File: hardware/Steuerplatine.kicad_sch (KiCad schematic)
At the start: 9 parts, among them J1 Conn_01x02_Pin, J2 Conn_01x02_Pin, J3 Conn_01x06_Pin

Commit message: done routing
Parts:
- removed J3: Conn_01x06_Pin, Connector_Phoenix_MC:PhoenixContact_MC_1,5_6-G-3.5_1x06_P3.50mm_Horizontal, symbol Connector:Conn_01x06_Pin
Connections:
- net L: now also J1.2 (Pin_2); no longer J1.1 (Pin_1)
- net N: now also J1.1 (Pin_1); no longer J1.2 (Pin_2)
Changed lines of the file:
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@@
 		)
 	)
-	(label "GND"
-		(at 254 124.46 180)
+	(label "+5V"
+		(at 245.11 21.59 0)
 		(fields_autoplaced yes)
 		(effects
@@
 				(size 1.27 1.27)
 			)
-			(justify right bottom)
-		)
-	)
-	(label "+5V"
-		(at 245.11 21.59 0)
+			(justify left bottom)
+		)
+	)
+	(label "L"
+		(at 245.11 29.21 0)
 		(fields_autoplaced yes)
 		(effects
@@
 	)
 	(label "+5V"
-		(at 254 127 180)
+		(at 41.91 21.59 0)
 		(fields_autoplaced yes)
 		(effects
@@
 				(size 1.27 1.27)
 			)
-			(justify right bottom)
-		)
-	)
-	(label "L"
-		(at 245.11 29.21 0)
-		(fields_autoplaced yes)
-		(effects
-			(font
-				(size 1.27 1.27)
-			)
-			(justify left bottom)
-		)
-	)
-	(label "+5V"
-		(at 41.91 21.59 0)
-		(fields_autoplaced yes)
-		(effects
-			(font
-				(size 1.27 1.27)
-			)
 			(justify left bottom)
 		)
@@
 	)
 	(symbol
-		(lib_id "Connector:Conn_01x06_Pin")
-		(at 259.08 121.92 180)
-		(unit 1)
-		(exclude_from_sim no)
-		(in_bom yes)
-		(on_board yes)
-		(dnp no)
-		(fields_autoplaced yes)
-		(property "Reference" "J3"
-			(at 260.35 119.3799 0)
-			(effects
-				(font
-					(size 1.27 1.27)
-				)
-				(justify right)
-			)
-		)
-		(property "Value" "Conn_01x06_Pin"
-			(at 260.35 121.9199 0)
-			(effects
-				(font
-					(size 1.27 1.27)
-				)
-				(justify right)
-			)
-		)
-		(property "Footprint" "Connector_Phoenix_MC:PhoenixContact_MC_1,5_6-G-3.5_1x06_P3.50mm_Horizontal"
-			(at 259.08 121.92 0)
-			(effects
-				(font
-					(size 1.27 1.27)
-				)
-				(hide yes)
-			)
-		)
-		(property "Datasheet" "~"
-			(at 259.08 121.92 0)
-			(effects
-				(font
-					(size 1.27 1.27)
-				)
-				(hide yes)
-			)
-		)
-		(property "Description" "Generic connector, single row, 01x06, script generated"
-			(at 259.08 121.92 0)
-			(effects
-				(font
-					(size 1.27 1.27)
-				)
-				(hide yes)
-			)
-		)
-		(pin "4"
-		)
-		(pin "3"
-		)
-		(pin "2"
-		)
-		(pin "1"
-		)
-		(pin "5"
-		)
-		(pin "6"
-		)
-		(instances
-			(project "Steuerplatine"
-				(path "/ae153005-c1c4-4678-92de-98a47cf88e8d"
-					(reference "J3")
-					(unit 1)
-				)
-			)
-		)
-	)
-	(symbol
 		(lib_id "Mechanical:MountingHole")
 		(at 16.51 193.04 0)
@@
 	(symbol
 		(lib_id "Connector:Conn_01x02_Pin")
-		(at 35.56 29.21 0)
+		(at 35.56 31.75 0)
+		(mirror x)
 		(unit 1)
 		(exclude_from_sim no)
@@
 		(dnp no)
 		(property "Reference" "J1"
-			(at 32.512 31.242 0)
+			(at 32.512 29.718 0)
 			(effects
 				(font
@@
 		)
 		(property "Value" "Conn_01x02_Pin"
-			(at 22.606 31.242 0)
+			(at 22.606 29.718 0)
 			(effects
 				(font
@@
 		)
 		(property "Footprint" "Connector_Phoenix_GMSTB:PhoenixContact_GMSTBA_2,5_2-G-7,62_1x02_P7.62mm_Horizontal"
-			(at 35.56 29.21 0)
-			(effects
-				(font
-					(size 1.27 1.27)
-				)
-				(hide yes)
-			)
-		)
-		(property "Datasheet" "~"
-			(at 35.56 29.21 0)
+			(at 35.56 31.75 0)
+			(effects
+				(font
+					(size 1.27 1.27)
+				)
+				(hide yes)
+			)
+		)
+		(property "Datasheet" "~"
+			(at 35.56 31.75 0)
 			(effects
 				(font
@@
 		)
 		(property "Description" "Generic connector, single row, 01x02, script generated"
-			(at 35.56 29.21 0)
-			(effects
-				(font
+			(at 35.56 31.75 0)
+			(effects
+				(font

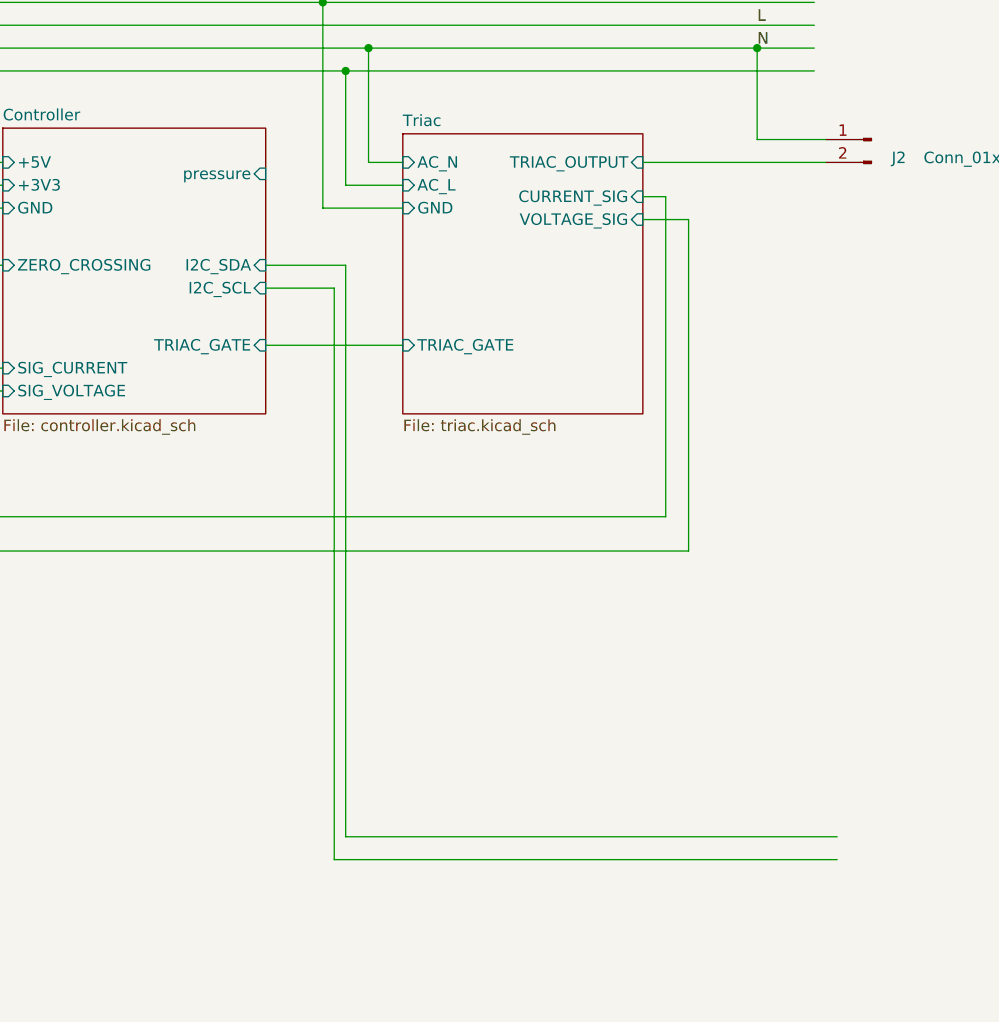
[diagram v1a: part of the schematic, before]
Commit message: added pressure sensor
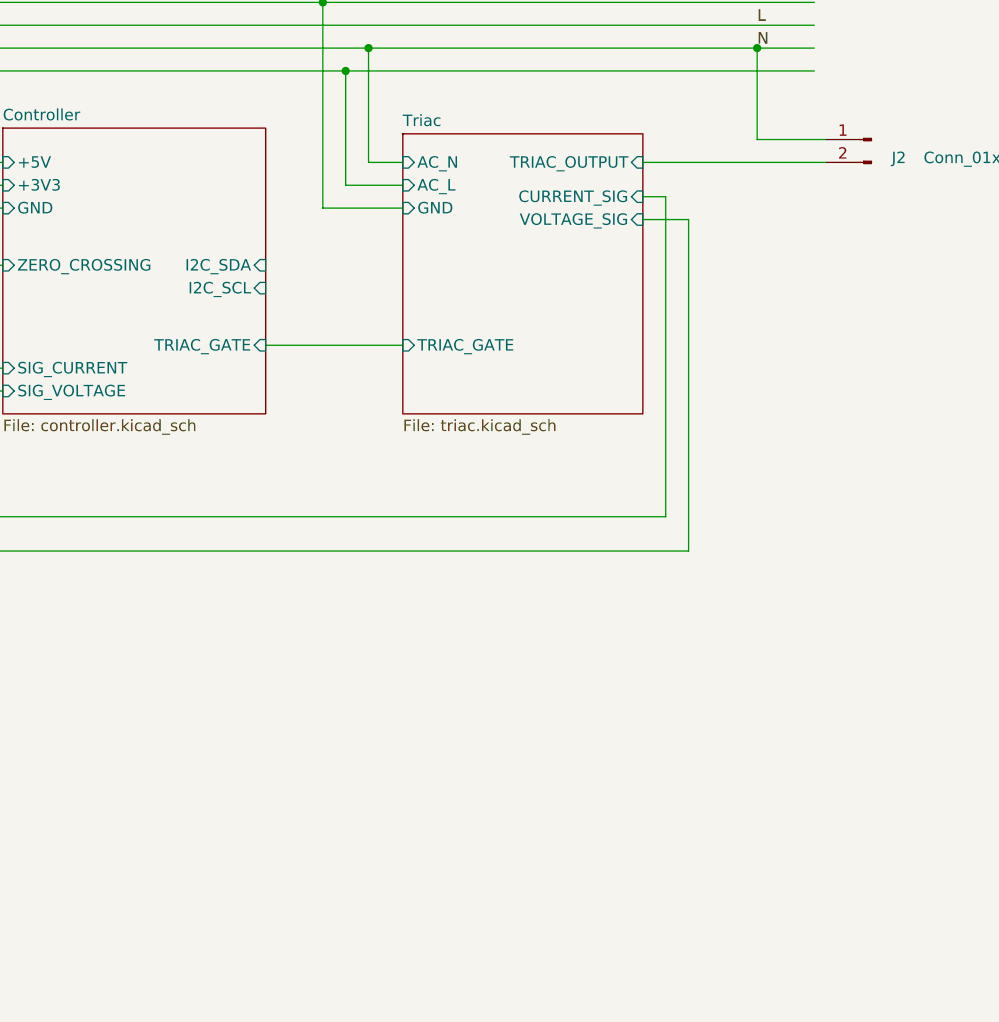
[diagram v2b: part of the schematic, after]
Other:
- sheet Controller ports: added none; removed pressure
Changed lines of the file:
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@@
-	(wire
-		(pts
-			(xy 190.5 58.42) (xy 198.12 58.42)
-		)
-		(stroke
-			(width 0)
-			(type default)
-		)
-	)
 	(wire
 		(pts
@@
 	(wire
 		(pts
-			(xy 190.5 55.88) (xy 199.39 55.88)
-		)
-		(stroke
-			(width 0)
-			(type default)
-		)
-	)
-	(wire
-		(pts
 			(xy 104.14 34.29) (xy 104.14 55.88)
 		)
@@
 	(wire
 		(pts
-			(xy 199.39 55.88) (xy 199.39 119.38)
-		)
-		(stroke
-			(width 0)
-			(type default)
-		)
-	)
-	(wire
-		(pts
-			(xy 198.12 121.92) (xy 254 121.92)
-		)
-		(stroke
-			(width 0)
-			(type default)
-		)
-	)
-	(wire
-		(pts
 			(xy 152.4 26.67) (xy 152.4 49.53)
 		)
@@
 	(wire
 		(pts
-			(xy 199.39 119.38) (xy 254 119.38)
-		)
-		(stroke
-			(width 0)
-			(type default)
-		)
-	)
-	(wire
-		(pts
 			(xy 40.64 34.29) (xy 76.2 34.29)
 		)
@@
 		(pts
 			(xy 237.49 87.63) (xy 158.75 87.63)
-		)
-		(stroke
-			(width 0)
-			(type default)
-		)
-	)
-	(wire
-		(pts
-			(xy 198.12 58.42) (xy 198.12 121.92)
 		)
 		(stroke
@@
 			)
 		)
-		(pin "pressure" input
-			(at 190.5 45.72 0)
-			(effects
-				(font
-					(size 1.27 1.27)
-				)
-				(justify right)
-			)
-		)

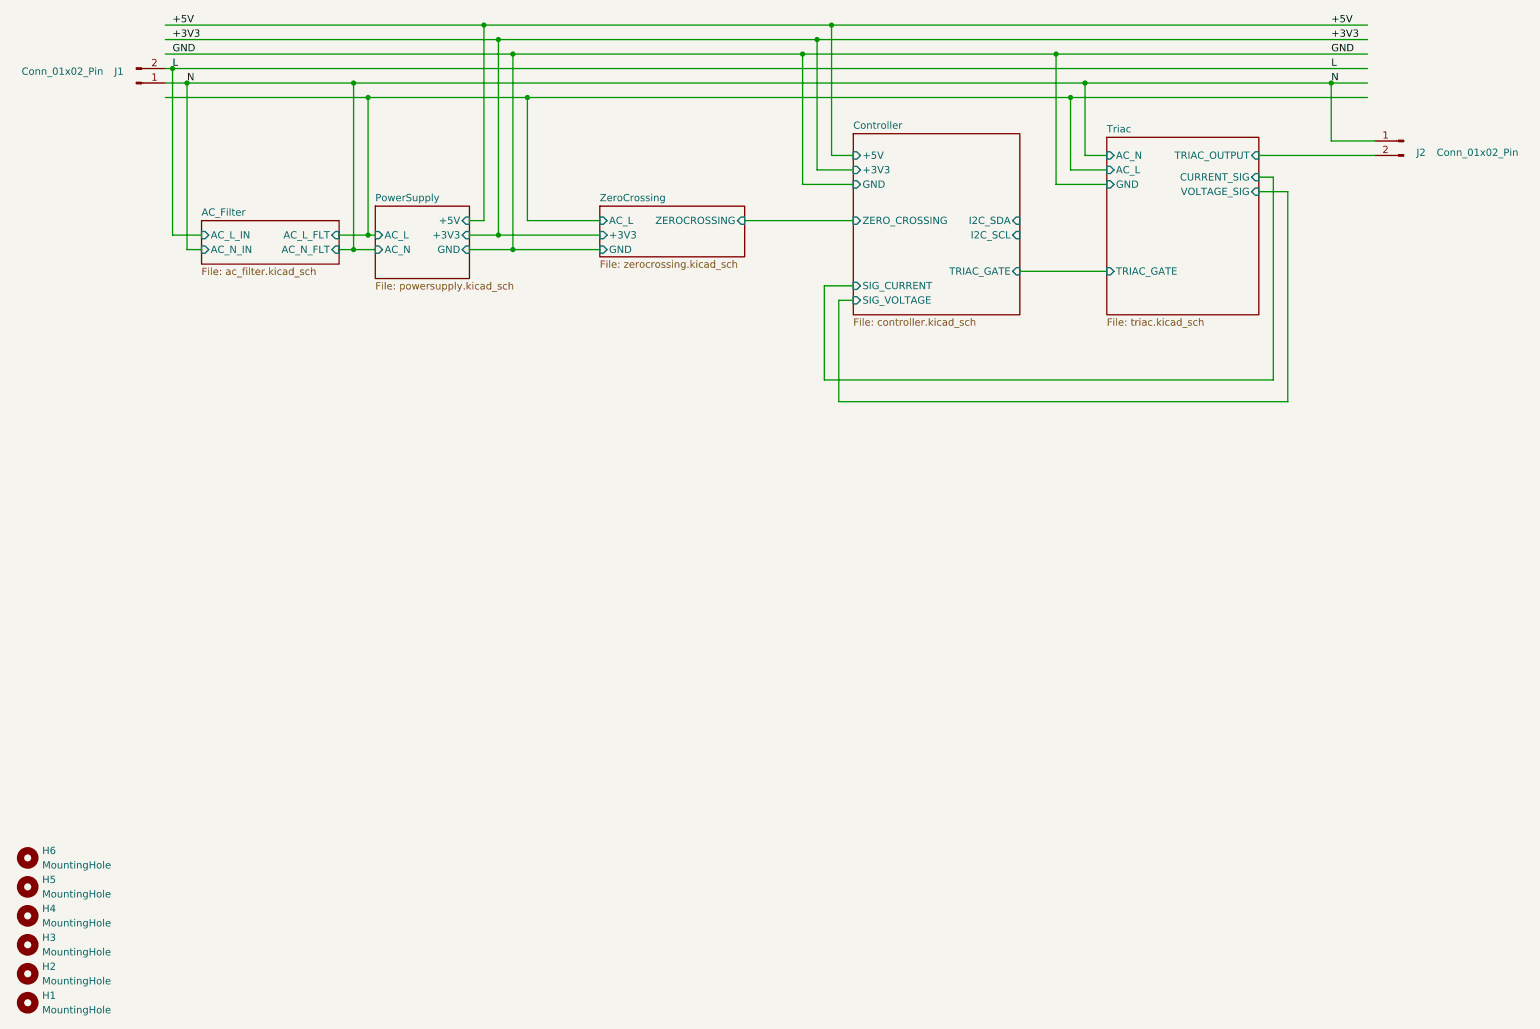
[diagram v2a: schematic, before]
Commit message: bugfix: triac output needs to confront L potential
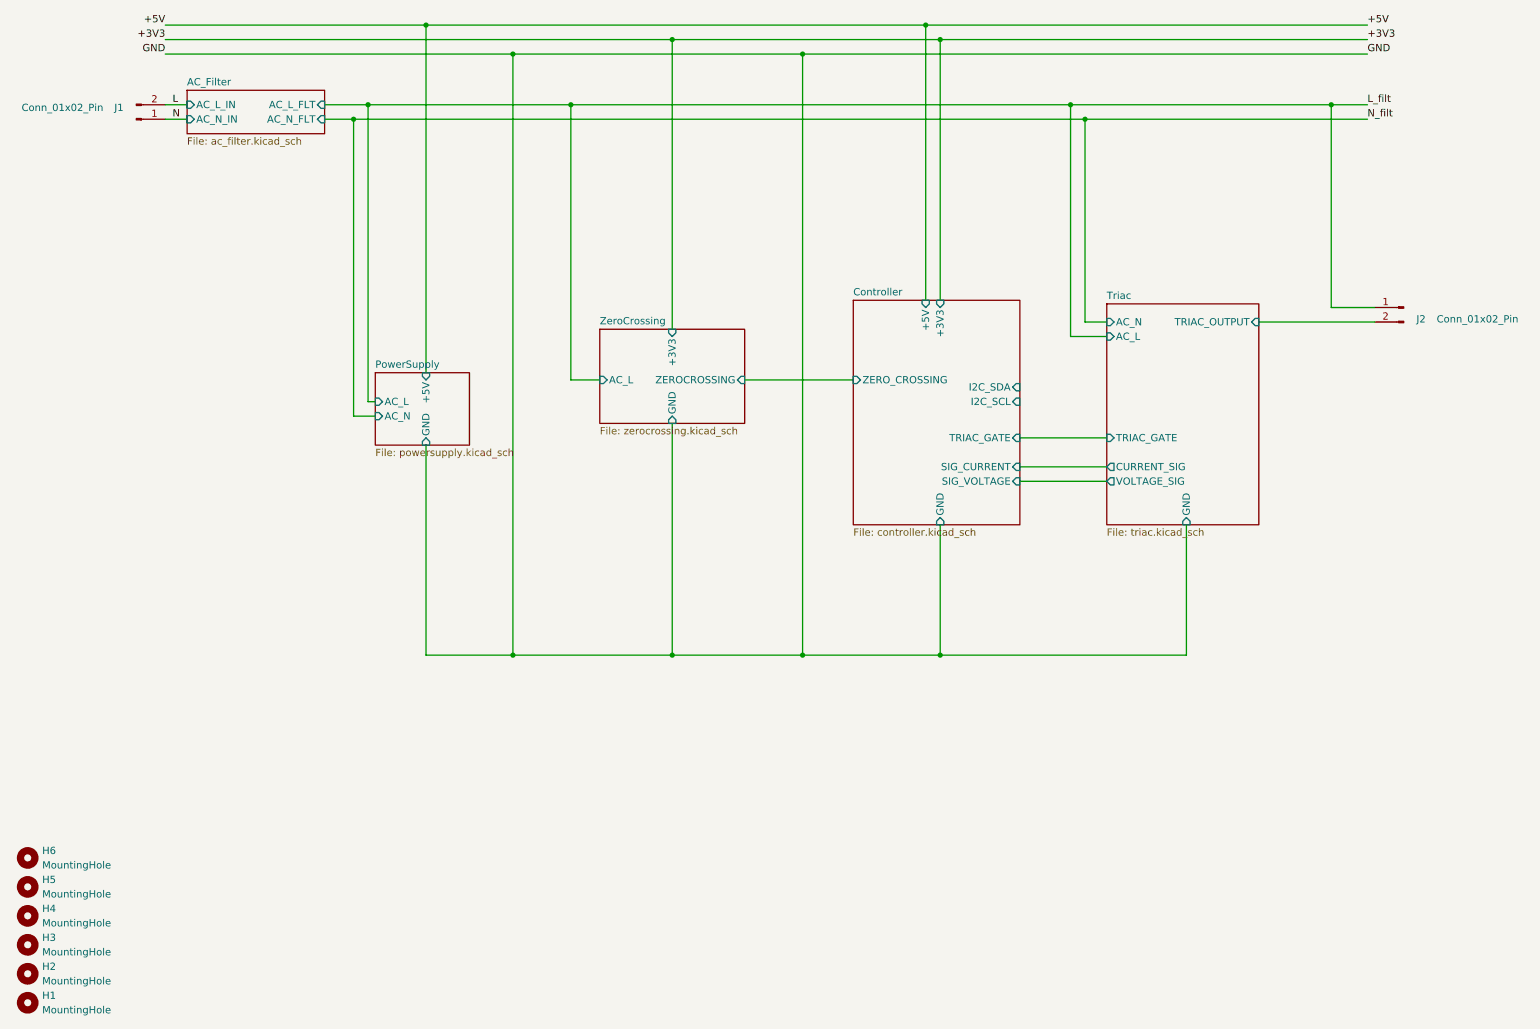
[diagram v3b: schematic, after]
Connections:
- net N: no longer J2.1 (Pin_1)
- new net L_filt: J2.1 (Pin_1)
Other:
- sheet PowerSupply ports: added none; removed +3V3
- moved on the sheet: J1, J2

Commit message: added some zones
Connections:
- net L: now also J1.1 (Pin_1); no longer J1.2 (Pin_2)
- net L_filt: now also J2.2 (Pin_2); no longer J2.1 (Pin_1)
- net N: now also J1.2 (Pin_2); no longer J1.1 (Pin_1)
- net Triac/TRIAC_OUTPUT: now also J2.1 (Pin_1); no longer J2.2 (Pin_2)
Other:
- moved on the sheet: J2
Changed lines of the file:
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@@
 	(symbol
 		(lib_id "Connector:Conn_01x02_Pin")
-		(at 257.81 71.12 0)
-		(mirror y)
+		(at 257.81 73.66 180)
 		(unit 1)
 		(exclude_from_sim no)
@@
 		(dnp no)
 		(property "Reference" "J2"
-			(at 260.858 73.152 0)
+			(at 260.858 71.628 0)
 			(effects
 				(font
@@
 		)
 		(property "Value" "Conn_01x02_Pin"
-			(at 270.764 73.152 0)
+			(at 270.764 71.628 0)
 			(effects
 				(font
@@
 		)
 		(property "Footprint" "Connector_Phoenix_GMSTB:PhoenixContact_GMSTBA_2,5_2-G-7,62_1x02_P7.62mm_Horizontal"
-			(at 257.81 71.12 0)
-			(effects
-				(font
-					(size 1.27 1.27)
-				)
-				(hide yes)
-			)
-		)
-		(property "Datasheet" "~"
-			(at 257.81 71.12 0)
+			(at 257.81 73.66 0)
+			(effects
+				(font
+					(size 1.27 1.27)
+				)
+				(hide yes)
+			)
+		)
+		(property "Datasheet" "~"
+			(at 257.81 73.66 0)
 			(effects
 				(font
@@
 		)
 		(property "Description" "Generic connector, single row, 01x02, script generated"
-			(at 257.81 71.12 0)
+			(at 257.81 73.66 0)
 			(effects
 				(font
@@
 	(symbol
 		(lib_id "Connector:Conn_01x02_Pin")
-		(at 35.56 38.1 0)
-		(mirror x)
+		(at 35.56 35.56 0)
 		(unit 1)
 		(exclude_from_sim no)
@@
 		(dnp no)
 		(property "Reference" "J1"
-			(at 32.512 36.068 0)
+			(at 32.512 37.592 0)
 			(effects
 				(font
@@
 		)
 		(property "Value" "Conn_01x02_Pin"
-			(at 22.606 36.068 0)
+			(at 22.606 37.592 0)
 			(effects
 				(font
@@
 		)
 		(property "Footprint" "Connector_Phoenix_GMSTB:PhoenixContact_GMSTBA_2,5_2-G-7,62_1x02_P7.62mm_Horizontal"
-			(at 35.56 38.1 0)
-			(effects
-				(font
-					(size 1.27 1.27)
-				)
-				(hide yes)
-			)
-		)
-		(property "Datasheet" "~"
-			(at 35.56 38.1 0)
+			(at 35.56 35.56 0)
+			(effects
+				(font
+					(size 1.27 1.27)
+				)
+				(hide yes)
+			)
+		)
+		(property "Datasheet" "~"
+			(at 35.56 35.56 0)
 			(effects
 				(font
@@
 		)
 		(property "Description" "Generic connector, single row, 01x02, script generated"
-			(at 35.56 38.1 0)
-			(effects
-				(font
+			(at 35.56 35.56 0)
+			(effects
+				(font

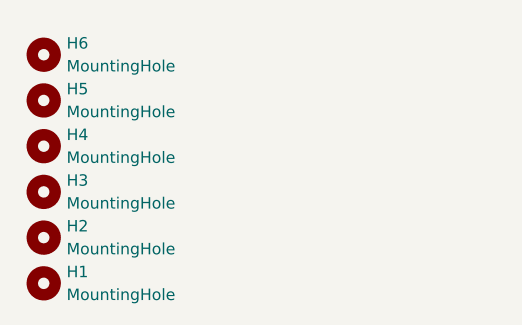
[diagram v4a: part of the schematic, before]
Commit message: some more rules and routings
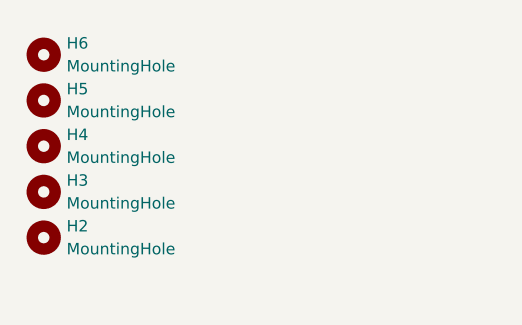
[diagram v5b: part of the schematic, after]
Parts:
- removed H1: MountingHole, MountingHole:MountingHole_3.5mm, symbol Mechanical:MountingHole
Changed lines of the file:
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@@
-	(symbol
-		(lib_id "Mechanical:MountingHole")
-		(at 16.51 193.04 0)
-		(unit 1)
-		(exclude_from_sim no)
-		(in_bom yes)
-		(on_board yes)
-		(dnp no)
-		(fields_autoplaced yes)
-		(property "Reference" "H1"
-			(at 19.05 191.7699 0)
-			(effects
-				(font
-					(size 1.27 1.27)
-				)
-				(justify left)
-			)
-		)
-		(property "Value" "MountingHole"
-			(at 19.05 194.3099 0)
-			(effects
-				(font
-					(size 1.27 1.27)
-				)
-				(justify left)
-			)
-		)
-		(property "Footprint" "MountingHole:MountingHole_3.5mm"
-			(at 16.51 193.04 0)
-			(effects
-				(font
-					(size 1.27 1.27)
-				)
-				(hide yes)
-			)
-		)
-		(property "Datasheet" "~"
-			(at 16.51 193.04 0)
-			(effects
-				(font
-					(size 1.27 1.27)
-				)
-				(hide yes)
-			)
-		)
-		(property "Description" "Mounting Hole without connection"
-			(at 16.51 193.04 0)
-			(effects
-				(font
-					(size 1.27 1.27)
-				)
-				(hide yes)
-			)
-		)
-		(instances
-			(project "Steuerplatine"
-				(path "/ae153005-c1c4-4678-92de-98a47cf88e8d"
-					(reference "H1")
-					(unit 1)
-				)
-			)
-		)
-	)
 	(symbol
 		(lib_id "Mechanical:MountingHole")
